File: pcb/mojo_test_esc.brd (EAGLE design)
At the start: 78.7 x 63.5 mm, 2 parts

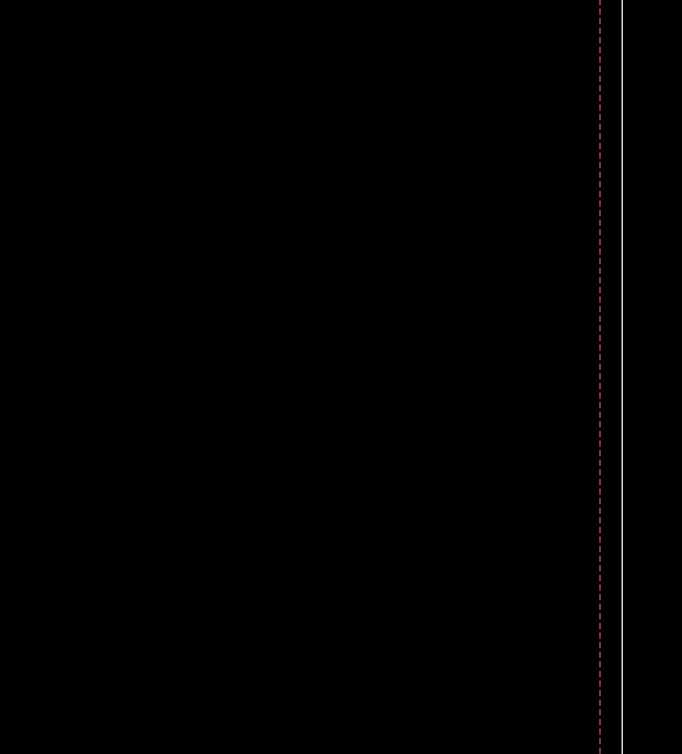
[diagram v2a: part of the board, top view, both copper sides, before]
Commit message: Adding SOT23 mosfet packages and associated datasheet
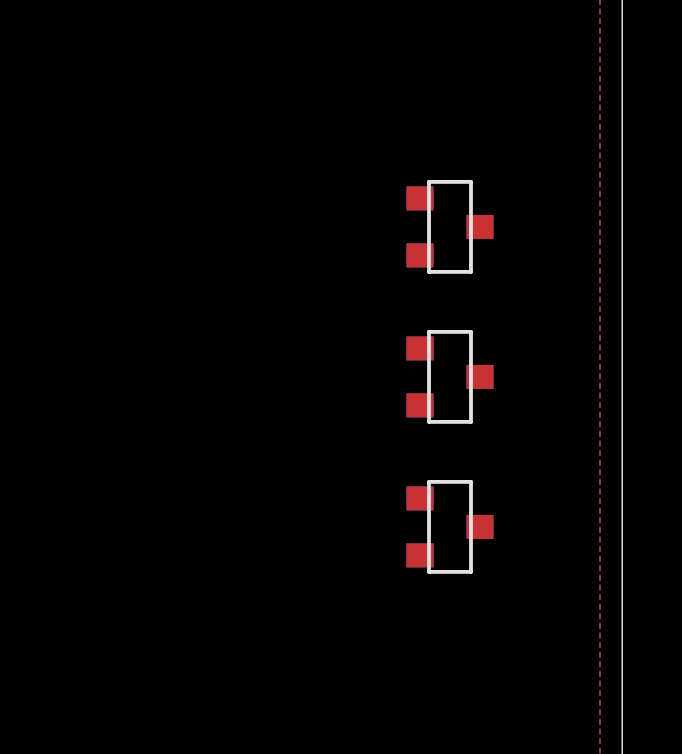
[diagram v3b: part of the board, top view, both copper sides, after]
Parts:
- added U$2, U$3, U$4, U$5, U$6, U$7: MOSFETSOT23, mojo_test_esc:SOT23
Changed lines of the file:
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@@
 <element name="B1" library="mojo_test_esc" package="MOJO_V3_NO_LABEL_NO_ANALOG" value="MOJO_NO_ANALOGV3_NO_LABEL" x="38.1" y="30.48"/>
 <element name="U$1" library="mojo_test_esc" package="DRV8302" value="DRV8302" x="49.5" y="38.83"/>
+<element name="U$2" library="mojo_test_esc" package="SOT23" value="MOSFETSOT23" x="73" y="48" rot="R270"/>
+<element name="U$3" library="mojo_test_esc" package="SOT23" value="MOSFETSOT23" x="73" y="43" rot="R270"/>
+<element name="U$4" library="mojo_test_esc" package="SOT23" value="MOSFETSOT23" x="73" y="38" rot="R270"/>
+<element name="U$5" library="mojo_test_esc" package="SOT23" value="MOSFETSOT23" x="73" y="48" rot="MR90"/>
+<element name="U$6" library="mojo_test_esc" package="SOT23" value="MOSFETSOT23" x="73" y="43" rot="MR90"/>
+<element name="U$7" library="mojo_test_esc" package="SOT23" value="MOSFETSOT23" x="73" y="38" rot="MR90"/>
 </elements>
 <signals>

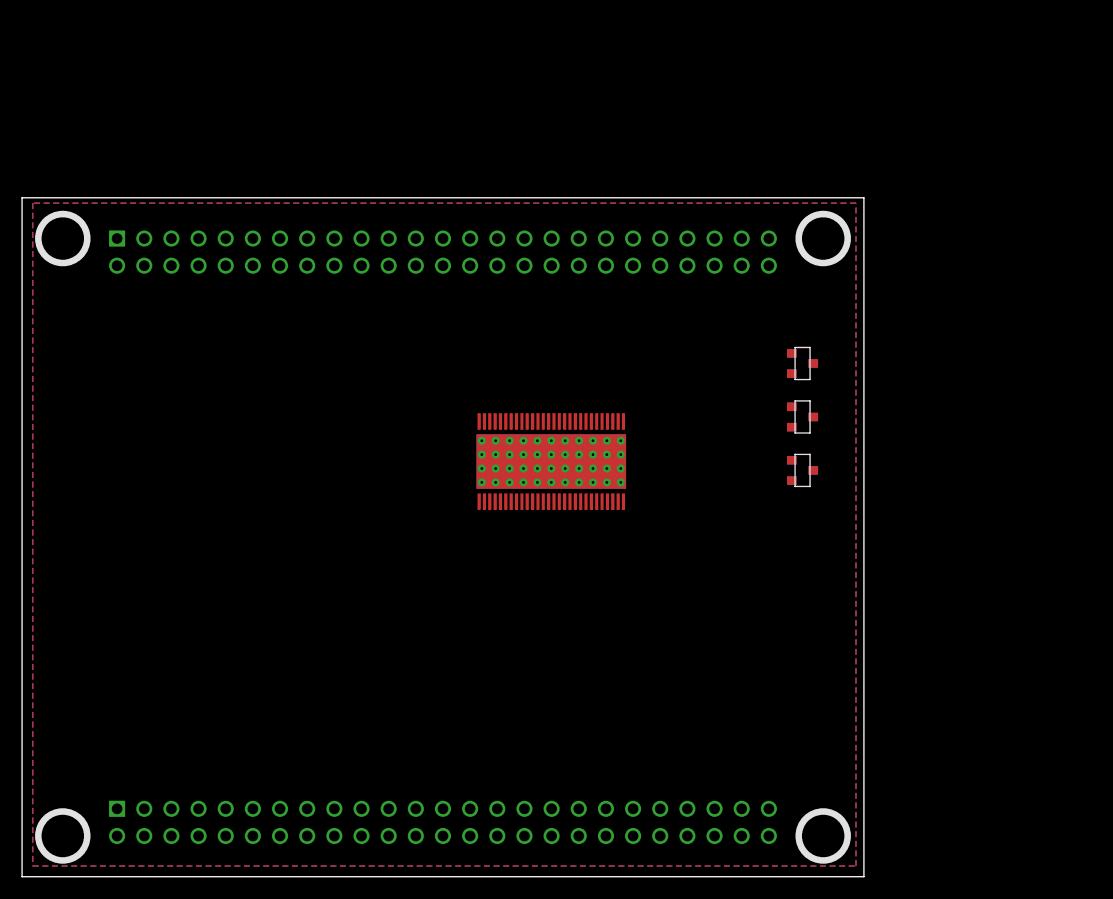
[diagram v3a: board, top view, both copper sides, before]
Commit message: Adding 8-pack resistor and updating MOSFETs again
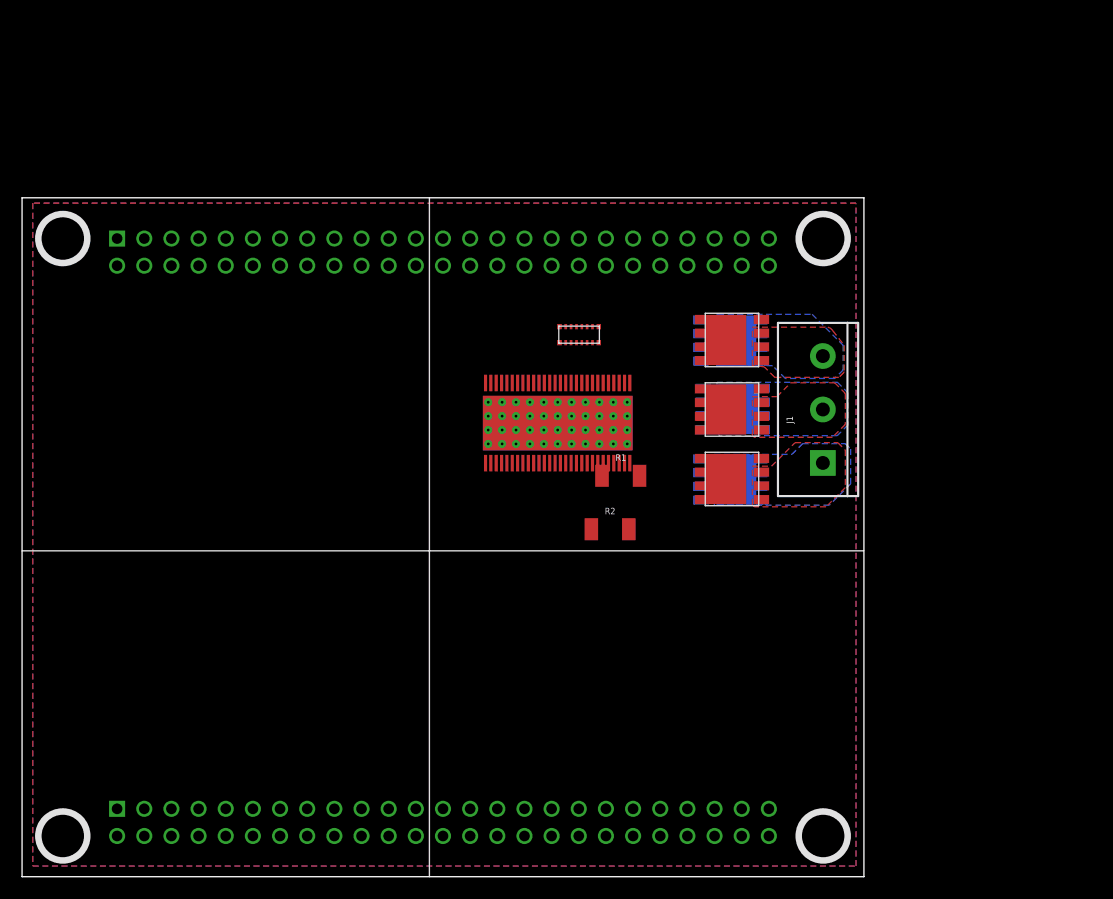
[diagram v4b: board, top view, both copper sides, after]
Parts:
- removed U$3, U$4, U$5, U$6, U$7: MOSFETSOT23, mojo_test_esc:SOT23
- added J1: (no value), SparkFun-Connectors:SCREWTERMINAL-5MM-3
- added MOSFET_H_A_1, MOSFET_H_B_1, MOSFET_H_C_1, MOSFET_L_A_1, MOSFET_L_B_1, MOSFET_L_C_1: MOSFET, mojo_test_esc:SOP_ADVANCE
- added R1, R2: 0.1, SparkFun-Resistors:1210
- U$2: value MOSFETSOT23 -> EXB2HV; device mojo_test_esc:SOT23 -> mojo_test_esc:EXB2HV
- moved U$2 21.1 mm to (52.1, 50.7), turned to 0 degrees
- moved U$1 3.65 mm to (50.1, 42.4)
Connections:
- new net +12V: MOSFET_H_A_1.P$5, MOSFET_H_A_1.P$6, MOSFET_H_A_1.P$7, MOSFET_H_A_1.P$8, MOSFET_H_A_1.P$9, MOSFET_H_B_1.P$5, MOSFET_H_B_1.P$6, MOSFET_H_B_1.P$7, MOSFET_H_B_1.P$8, MOSFET_H_B_1.P$9, MOSFET_H_C_1.P$5, MOSFET_H_C_1.P$6, MOSFET_H_C_1.P$7, MOSFET_H_C_1.P$8, MOSFET_H_C_1.P$9
- new net GH_A: MOSFET_H_A_1.P$4, U$2.P2B
- new net GH_B: MOSFET_H_B_1.P$4, U$2.P4B
- new net GH_C: MOSFET_H_C_1.P$4, U$2.P6B
- new net GL_A: MOSFET_L_A_1.P$4, U$2.P3B
- new net GL_B: MOSFET_L_B_1.P$4, U$2.P5B
- new net GL_C: MOSFET_L_C_1.P$4, U$2.P7B
- new net N$1: U$1.P$47, U$2.P2
- new net N$2: U$1.P$45, U$2.P3
- new net N$3: U$1.P$42, U$2.P4
- new net N$4: U$1.P$40, U$2.P5
- new net N$5: U$1.P$37, U$2.P6
- new net N$6: U$1.P$35, U$2.P7
- new net SH_A: J1.3, MOSFET_H_A_1.P$1, MOSFET_H_A_1.P$2, MOSFET_H_A_1.P$3, MOSFET_L_A_1.P$5, MOSFET_L_A_1.P$6, MOSFET_L_A_1.P$7, MOSFET_L_A_1.P$8, MOSFET_L_A_1.P$9
- new net SH_B: J1.2, MOSFET_H_B_1.P$1, MOSFET_H_B_1.P$2, MOSFET_H_B_1.P$3, MOSFET_L_B_1.P$5, MOSFET_L_B_1.P$6, MOSFET_L_B_1.P$7, MOSFET_L_B_1.P$8, MOSFET_L_B_1.P$9
- new net SH_C: J1.1, MOSFET_H_C_1.P$1, MOSFET_H_C_1.P$2, MOSFET_H_C_1.P$3, MOSFET_L_C_1.P$5, MOSFET_L_C_1.P$6, MOSFET_L_C_1.P$7, MOSFET_L_C_1.P$8, MOSFET_L_C_1.P$9
- new net SL_A: MOSFET_L_A_1.P$1, MOSFET_L_A_1.P$2, MOSFET_L_A_1.P$3, R1.2
- new net SL_B: MOSFET_L_B_1.P$1, MOSFET_L_B_1.P$2, MOSFET_L_B_1.P$3, R2.2
- net GND: now also MOSFET_L_C_1.P$1, MOSFET_L_C_1.P$2, MOSFET_L_C_1.P$3, R1.1, R2.1
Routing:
- added copper zone on layer 1, net SH_A
- added copper zone on layer 16, net SH_A
- added copper zone on layer 1, net SH_B
- added copper zone on layer 16, net SH_B
- added copper zone on layer 1, net SH_C
- added copper zone on layer 16, net SH_C
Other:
- board text added: "A"
- board text added: "B"
- board text added: "C"

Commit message: Initial layout with capacitors
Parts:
- added C1, C3, C4, C5, C7, C9: 0.1uF, SparkFun-Capacitors:0402
- added C10: 47uF, SparkFun-Capacitors:EIA3528
- added C11: 10uF, SparkFun-Capacitors:0603
- added C12: 100PF, SparkFun-Capacitors:0402
- added C13, C17, C18: 2.2uF, SparkFun-Capacitors:0603
- added C14, C6: 22nF, SparkFun-Capacitors:0603
- added C15, C16: 1.0uF, SparkFun-Capacitors:0402
- added C2, C8: 4.7uF, SparkFun-Capacitors:0603
- added D1: 250mA/100V, SparkFun-DiscreteSemi:SOD-323
- added L1: 47µH/±30%/750mA, SparkFun-Coils:CR54
- added R10, R5, R6, R9: 10k, SparkFun-Resistors:0603
- added R11: 1, SparkFun-Resistors:0603
- added R12, R13: 68OHM-0603-1/10W-1%, SparkFun-Resistors:0603
- added R3: 16.2k, SparkFun-Resistors:0603
- added R4: 33k, SparkFun-Resistors:0603
- added R7, R8: CSM2512, mojo_test_esc:CSM2512
- R1: value 0.1 -> 1M; device SparkFun-Resistors:1210 -> SparkFun-Resistors:0603
- R2: value 0.1 -> 200k; device SparkFun-Resistors:1210 -> SparkFun-Resistors:0603
- moved R1 27.2 mm to (42.2, 14.0)
- moved R2 17.6 mm to (58.6, 49.7)
- moved U$2 15.0 mm to (47.5, 36.4), flipped to the bottom
- moved U$1 3.08 mm to (47.8, 44.4), turned to 180 degrees
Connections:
- new net AGND: C15.1, C16.1, U$1.P$28
- new net DC_CAL: U$1.P$12
- new net EN_GATE: U$1.P$16
- new net GAIN: U$1.P$10
- new net GL_A_BEF_RES: U$1.P$45, U$2.P3B
- new net INH_A: U$1.P$17
- new net INH_B: U$1.P$19
- new net INH_C: U$1.P$21
- new net INL_A: U$1.P$18
- new net INL_B: U$1.P$20
- new net INL_C: U$1.P$22
- new net M_OC: U$1.P$9
- new net M_PWM: U$1.P$8
- new net N$10: C9.1, U$1.P$52
- new net N$11: C9.2, D1.C, L1.P$1, U$1.P$50, U$1.P$51
- new net N$12: R2.2, U$1.P$1
- new net N$13: R1.1, U$1.P$49
- new net N$14: C12.1, R3.2, U$1.P$2
- new net N$15: C11.1, R3.1
- new net N$16: R11.2, U$1.P$7
- new net N$17: C13.2, U$1.P$13
- new net N$18: C14.1, U$1.P$14
- new net N$19: R10.2, R4.1, U$1.P$3
- new net N$20: C14.2, U$1.P$15
- new net N$21: C15.2, U$1.P$23
- new net N$22: C16.2, U$1.P$27
- new net N$23: R12.2, U$1.P$25
- new net N$24: R13.2, U$1.P$26
- new net N$7: C3.1, U$1.P$48
- new net N$8: C4.1, U$1.P$43
- new net N$9: C5.1, U$1.P$38
- new net NFAULT: R9.1, U$1.P$6
- new net NOCTW: R6.1, U$1.P$5
- new net OC_ADJ: U$1.P$11
- new net PWRGD: R5.1, U$1.P$4
- new net REF: U$1.P$24
- new net SO1: R12.1
- new net SO2: C17.1, C18.1, R13.1
- new net VCC: C10.A, L1.P$2, R4.2, R5.2, R6.2, R9.2
- net +12V: now also C1.1, C2.1, C7.1, C8.1, U$1.P$29, U$1.P$53, U$1.P$54
- net GH_A: no longer U$2.P2B
- net GH_B: no longer U$2.P4B
- net GH_C: no longer U$2.P6B
- net GL_A: no longer U$2.P3B
- net GL_B: no longer U$2.P5B
- net GL_C: no longer U$2.P7B
- net GND: now also C1.2, C10.C, C11.2, C12.2, C13.1, C17.2, C18.2, C2.2, C6.2, C7.2, C8.2, D1.A, R1.2, R10.1, R11.1, R7.P1L, R7.P2L, R8.P1L, R8.P2L, U$1.P$30, U$1.P$32, U$1.P$34; no longer R1.1
- net N$1: now also U$2.P2B; no longer U$2.P2
- net N$2: now also C6.1, U$1.P$56; no longer U$1.P$45, U$2.P3
- net N$3: now also U$2.P4B; no longer U$2.P4
- net N$4: now also U$2.P5B; no longer U$2.P5
- net N$5: now also U$2.P6B; no longer U$2.P6
- net N$6: now also U$2.P7B; no longer U$2.P7
- net SH_A: now also C3.2, U$1.P$46
- net SH_B: now also C4.2, U$1.P$41
- net SH_C: now also C5.2, U$1.P$36
- net SL_A: now also R7.P1R, R7.P2R, U$1.P$33, U$1.P$44; no longer R1.2
- net SL_B: now also R8.P1R, R8.P2R, U$1.P$31, U$1.P$39; no longer R2.2
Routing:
- net N$6: track 0.00 -> 5.27 mm, vias 0 -> 1
- net N$5: track 0.00 -> 4.25 mm, vias 0 -> 1
- net N$1: track 0.00 -> 4.25 mm, vias 0 -> 1
- net N$4: track 0.00 -> 3.93 mm, vias 0 -> 1
- net GL_A_BEF_RES: track 0.00 -> 3.85 mm, vias 0 -> 1
- net N$3: track 0.00 -> 3.63 mm, vias 0 -> 1
- net N$9: track 0.00 -> 2.81 mm
- net N$7: track 0.00 -> 2.67 mm
- net N$8: track 0.00 -> 2.66 mm
- net SH_B: track 0.00 -> 2.44 mm
- net SH_C: track 0.00 -> 2.42 mm
- net SH_A: track 0.00 -> 2.40 mm
- added copper zone on layer 16, net SL_A
- added copper zone on layer 16, net SL_B
